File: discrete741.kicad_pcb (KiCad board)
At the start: 2 copper layers, 10.2 x 7.6 mm, 33 parts, among them J1 DIP-8 Pins, Q1 CET3904E, Q10 CET3904E, Q11 CET3904E, Q12 CET3906E, Q13 CET3906E, Q14 CET3904E, Q15 CET3904E, Q16 CET3904E, Q17 CET3904E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

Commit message: cosmetic changes
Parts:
- moved Q13 5.41 mm to (77.1, 71.3)
- moved Q16 5.41 mm to (82.5, 72.3)
- moved Q9 5.41 mm to (77.1, 73.5)
- moved R3 5.41 mm to (85.6, 75.0)
- moved J1 5.41 mm to (77.5, 76.2)
- moved Q10 5.41 mm to (80.8, 72.4)
- moved Q11 5.41 mm to (85.8, 71.3)
- moved Q12 5.41 mm to (77.4, 72.4)
- moved Q14 5.41 mm to (77.4, 70.1)
- moved Q2 5.41 mm to (78.9, 74.7)
- moved Q7 5.41 mm to (82.5, 74.7)
- moved R10 5.41 mm to (83.7, 69.4)
- moved R11 5.41 mm to (85.6, 70.2)
- moved R5 5.41 mm to (78.9, 70.0)
- moved Q15 5.41 mm to (80.5, 71.3)
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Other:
- outline, holes or cut-outs redrawn
- board text added: "MAGIC DORITO Discrete 741 DIP-8 ettingersam@gmail"

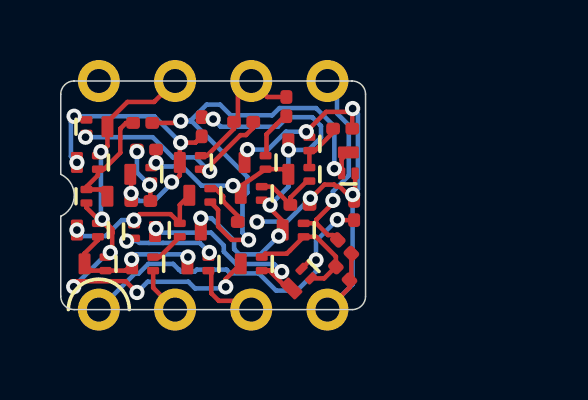
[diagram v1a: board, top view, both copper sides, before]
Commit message: Added mark to distinguish NPN and PNP BJTs
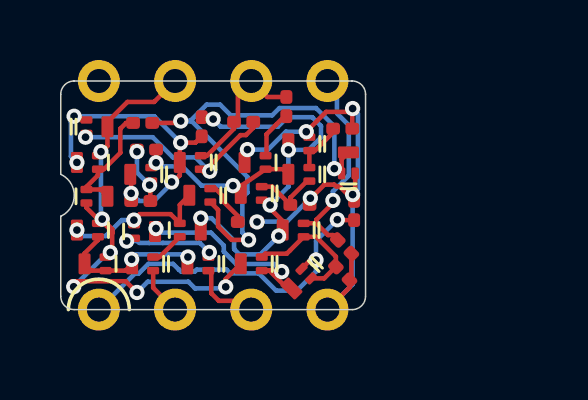
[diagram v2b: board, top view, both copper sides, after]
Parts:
- Q1, Q10, Q11, Q14, Q15, Q16, Q17, Q18, Q2, Q22, Q5, Q6, Q7: footprint discrete741:SOT-883 -> discrete741:SOT-883L-alt
- Q12, Q13, Q20, Q3, Q4, Q8, Q9: footprint discrete741:SOT-883 -> discrete741:SOT-883L

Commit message: Added diodes per latest version of EMSL kit
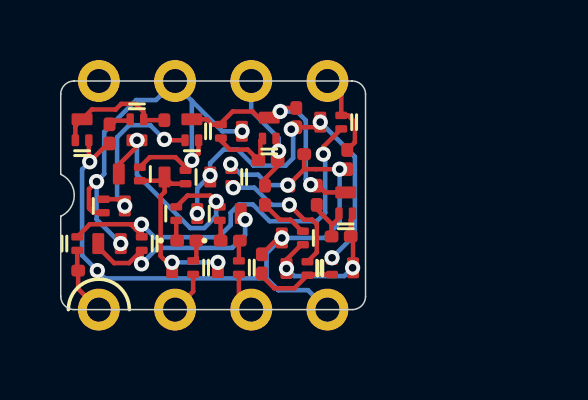
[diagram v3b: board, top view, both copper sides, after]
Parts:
- added D1: D_Schottky, Diode_SMD:D_0201_0603Metric, F.Cu at (81.8, 73.9)
- added D2: D_Schottky, Diode_SMD:D_0201_0603Metric, F.Cu at (80.4, 73.9)
- moved R1 9.10 mm to (77.1, 74.9), turned to 0 degrees
- moved Q11 8.95 mm to (76.9, 70.2)
- moved Q5 7.15 mm to (77.1, 74.0), turned to 0 degrees
- moved R8 7.11 mm to (85.5, 73.8)
- moved Q18 6.90 mm to (85.7, 72.6), turned to 90 degrees
- moved R7 5.87 mm to (84.7, 72.4), turned to 270 degrees
- moved R4 5.45 mm to (77.8, 70.3), turned to 270 degrees
- moved Q14 4.49 mm to (81.9, 70.3)
- moved R3 4.09 mm to (84.6, 71.0), turned to 180 degrees
- moved Q7 4.06 mm to (78.5, 74.0)
- moved Q8 3.94 mm to (80.0, 71.8)
- moved Q16 3.93 mm to (85.6, 74.8), turned to 0 degrees
- moved Q6 3.81 mm to (85.2, 70.0)
- moved Q13 3.65 mm to (80.6, 70.2), turned to 90 degrees
- moved C1 3.17 mm to (84.0, 69.8), turned to 270 degrees
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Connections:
- Q1 pad 2: Net-(Q1-Pad2) -> Net-(D1-Pad2)
- Q2 pad 2: Net-(Q2-Pad2) -> Net-(D2-Pad2)
- Q3 pad 2: Net-(Q1-Pad2) -> Net-(D1-Pad1)
- Q4 pad 2: Net-(Q2-Pad2) -> Net-(D2-Pad1)
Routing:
- net Net-(Q10-Pad1): track 16.7 -> 4.11 mm, vias 3 -> 0
- net Offset1: track 11.9 -> 2.27 mm, vias 2 -> 0
- net Net-(Q5-Pad1): track 4.35 -> 13.7 mm, vias 0 -> 2
- net Vcc-: track 20.3 -> 25.6 mm
- net Net-(Q14-Pad2): track 7.58 -> 2.38 mm, vias 2 -> 0
- net Offset2: track 6.91 -> 2.92 mm, vias 1 -> 0
- net Net-(Q1-Pad2): track 3.37 -> 0.00 mm, vias 2 -> 0
- net Net-(Q10-Pad3): track 5.16 -> 8.52 mm
- net Net-(Q17-Pad2): track 1.74 -> 4.87 mm, vias 0 -> 2
- net Net-(C1-Pad1): track 11.0 -> 8.45 mm, vias 5 -> 2
- net Net-(Q12-Pad1): track 3.91 -> 5.83 mm, vias 0 -> 2
- net Net-(C1-Pad2): track 14.1 -> 12.6 mm
- net Net-(Q1-Pad3): track 5.07 -> 6.45 mm
- net Net-(Q2-Pad2): track 1.17 -> 0.00 mm
- net Vcc+: track 18.1 -> 17.0 mm, vias 6 -> 4
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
